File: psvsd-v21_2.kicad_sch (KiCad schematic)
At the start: 28 parts, among them J1 MEM2075-00-140-01-A, U1 RP2040, U4 W25Q32JVZP, X1 ABM8-272-T3

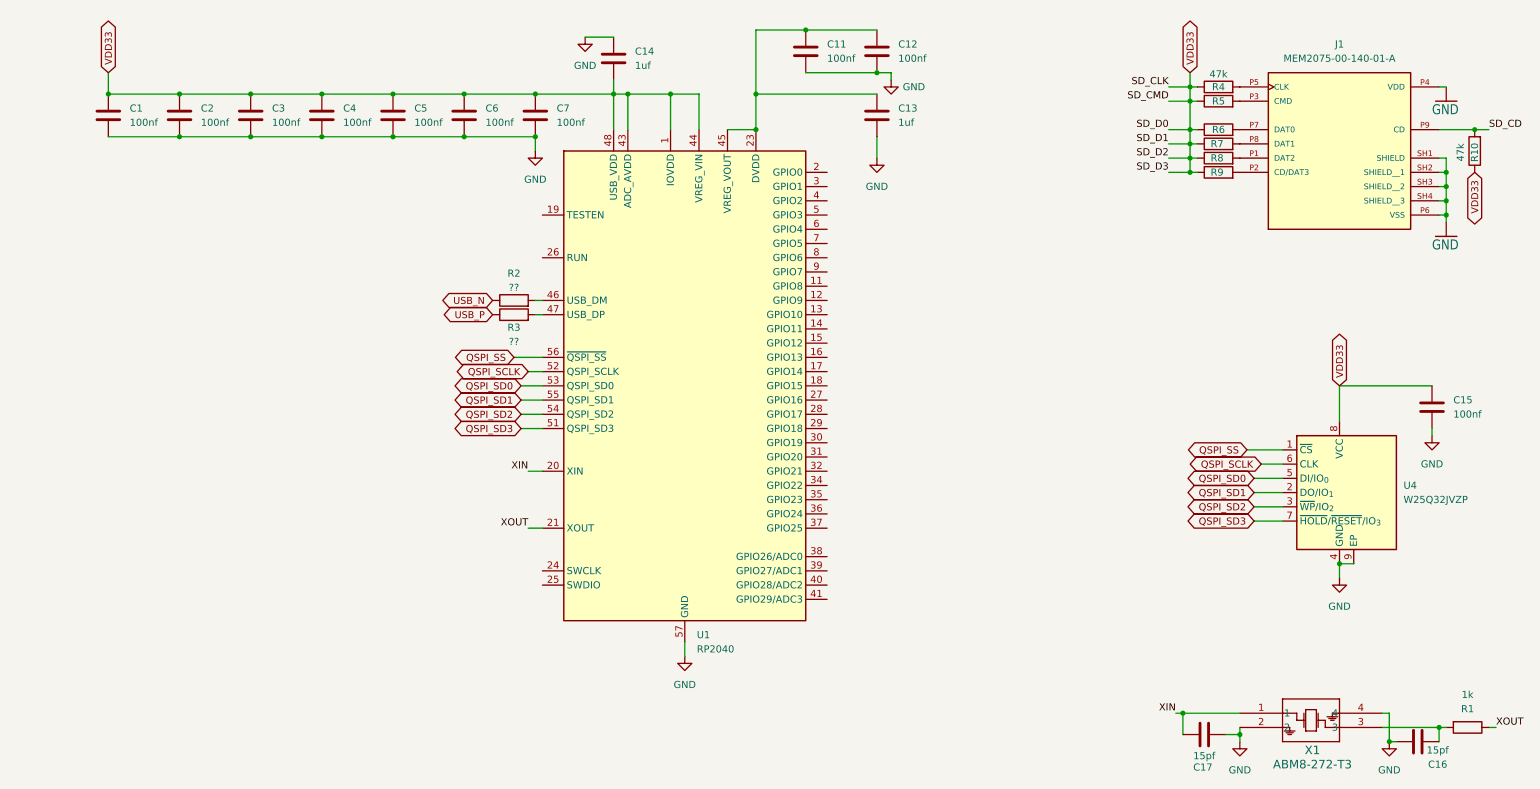
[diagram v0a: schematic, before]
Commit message: Add UART and SWDIO debug headers (plus delete some accidental junk files)
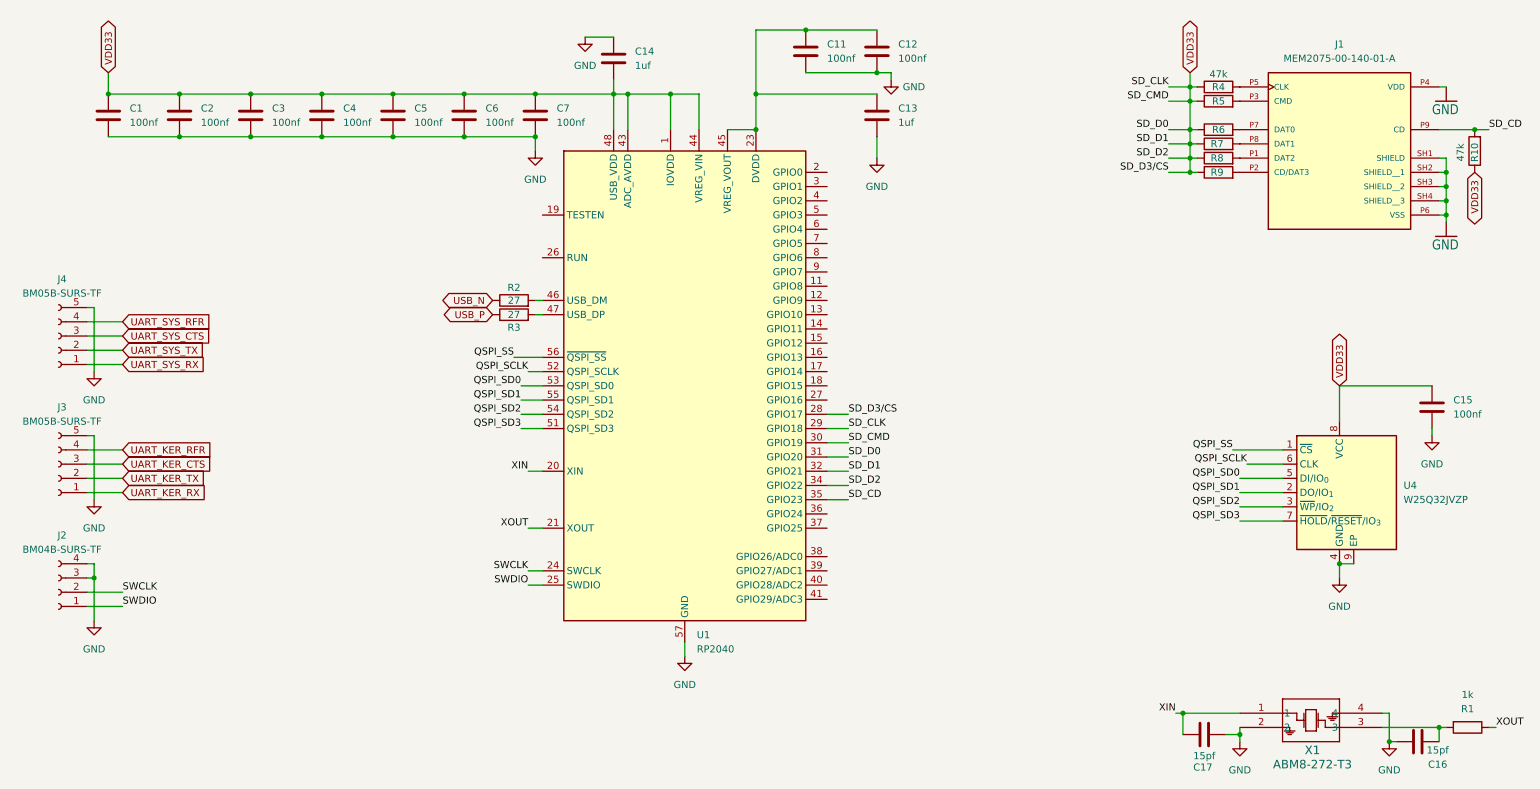
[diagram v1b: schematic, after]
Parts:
- added J2: BM04B-SURS-TF, Connector_JST:JST_SUR_BM04B-SURS-TF_1x04-1MP_P0.80mm_Vertical, symbol Connector:Conn_01x04_Socket
- added J3, J4: BM05B-SURS-TF, Connector_JST:JST_SUR_BM05B-SURS-TF_1x05-1MP_P0.80mm_Vertical, symbol Connector:Conn_01x05_Socket
- R2, R3: value ?? -> 27
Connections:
- net GND: now also J2.3 (Pin_3), J2.4 (Pin_4), J3.5 (Pin_5), J4.5 (Pin_5)
- net SD_CD: now also U1.35 (GPIO23)
- net VDD33: now also U1.28 (GPIO17), U1.29 (GPIO18), U1.30 (GPIO19), U1.31 (GPIO20), U1.32 (GPIO21), U1.34 (GPIO22)
- net SWCLK: now reaches U1.24 (SWCLK)
- net SWCLK: now also J2.2 (Pin_2)
- net SWDIO: now reaches U1.25 (SWDIO)
- net SWDIO: now also J2.1 (Pin_1)
- new net UART_KER_CTS: J3.3 (Pin_3)
- new net UART_KER_RFR: J3.4 (Pin_4)
- new net UART_KER_RX: J3.1 (Pin_1)
- new net UART_KER_TX: J3.2 (Pin_2)
- new net UART_SYS_CTS: J4.3 (Pin_3)
- new net UART_SYS_RFR: J4.4 (Pin_4)
- new net UART_SYS_RX: J4.1 (Pin_1)
- new net UART_SYS_TX: J4.2 (Pin_2)

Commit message: Connect Kermit and Syscon debug headers
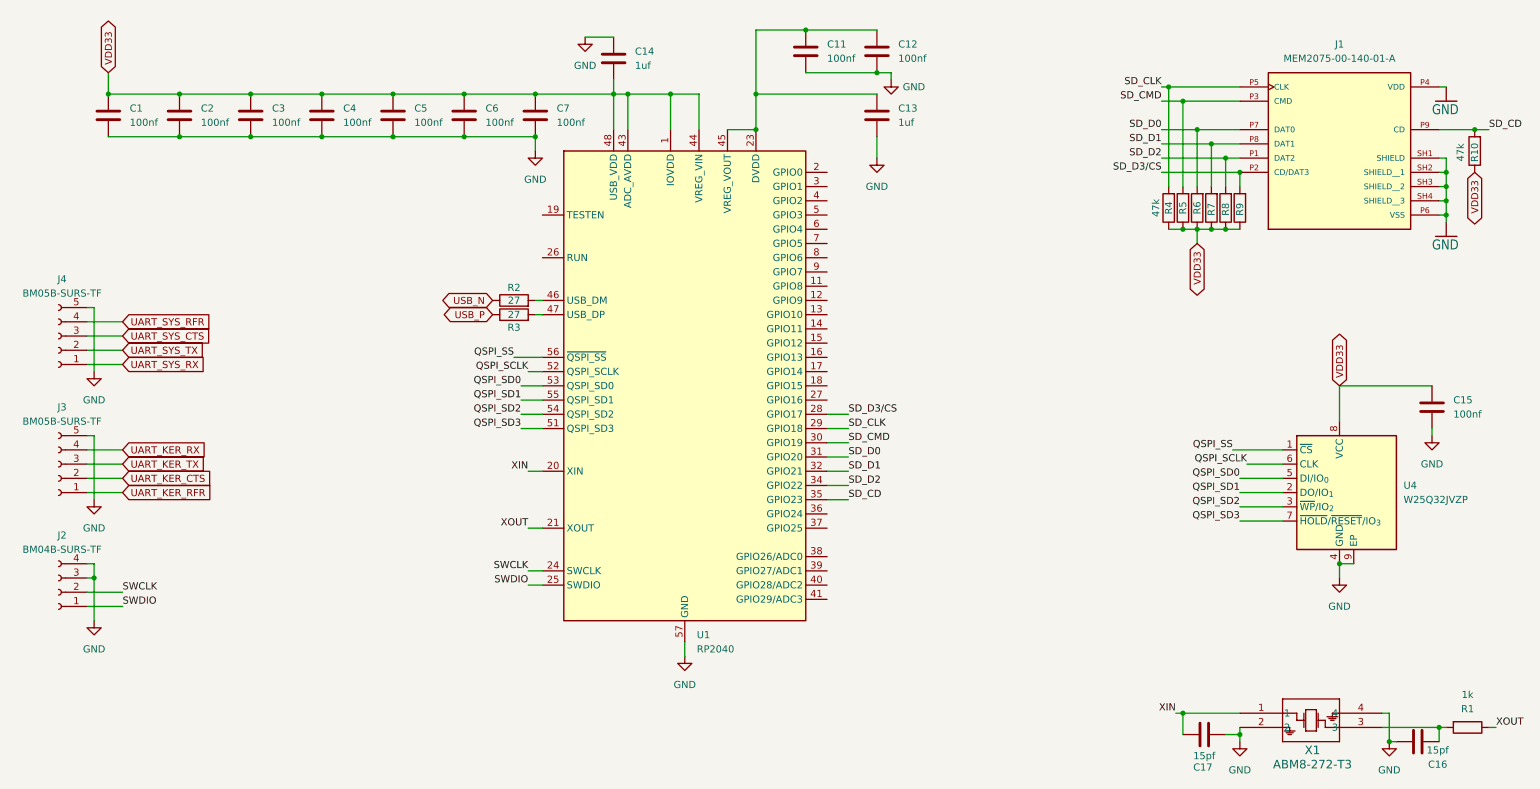
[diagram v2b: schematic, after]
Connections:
- net UART_KER_CTS: now also J3.2 (Pin_2); no longer J3.3 (Pin_3)
- net UART_KER_RFR: now also J3.1 (Pin_1); no longer J3.4 (Pin_4)
- net UART_KER_RX: now also J3.4 (Pin_4); no longer J3.1 (Pin_1)
- net UART_KER_TX: now also J3.3 (Pin_3); no longer J3.2 (Pin_2)
- net VDD33: no longer U1.28 (GPIO17), U1.29 (GPIO18), U1.30 (GPIO19), U1.31 (GPIO20), U1.32 (GPIO21), U1.34 (GPIO22)
- net SD_D2: now reaches J1.P1 (DAT2), R8.2
- net SD_D2: now also U1.34 (GPIO22)
- net SD_D0: now reaches J1.P7 (DAT0), R6.2
- net SD_D0: now also U1.31 (GPIO20)
- net SD_D3/CS: now reaches J1.P2 (CD/DAT3), R9.2
- net SD_D3/CS: now also U1.28 (GPIO17)
- net SD_CLK: now reaches J1.P5 (CLK), R4.2
- net SD_CLK: now also U1.29 (GPIO18)
- net SD_CMD: now reaches J1.P3 (CMD), R5.2
- net SD_CMD: now also U1.30 (GPIO19)
- net SD_D1: now reaches J1.P8 (DAT1), R7.2
- net SD_D1: now also U1.32 (GPIO21)
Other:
- moved on the sheet: R4, R5, R6, R7, R8, R9

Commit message: Fix wrong resistor package
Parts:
- R10: footprint Resistor_SMD:R_0402_1005Metric -> Resistor_SMD:R_01005_0402Metric
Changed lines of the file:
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@@
 			)
 		)
-		(property "Footprint" "Resistor_SMD:R_0402_1005Metric"
+		(property "Footprint" "Resistor_SMD:R_01005_0402Metric"
 			(at 277.368 39.37 90)
 			(hide yes)

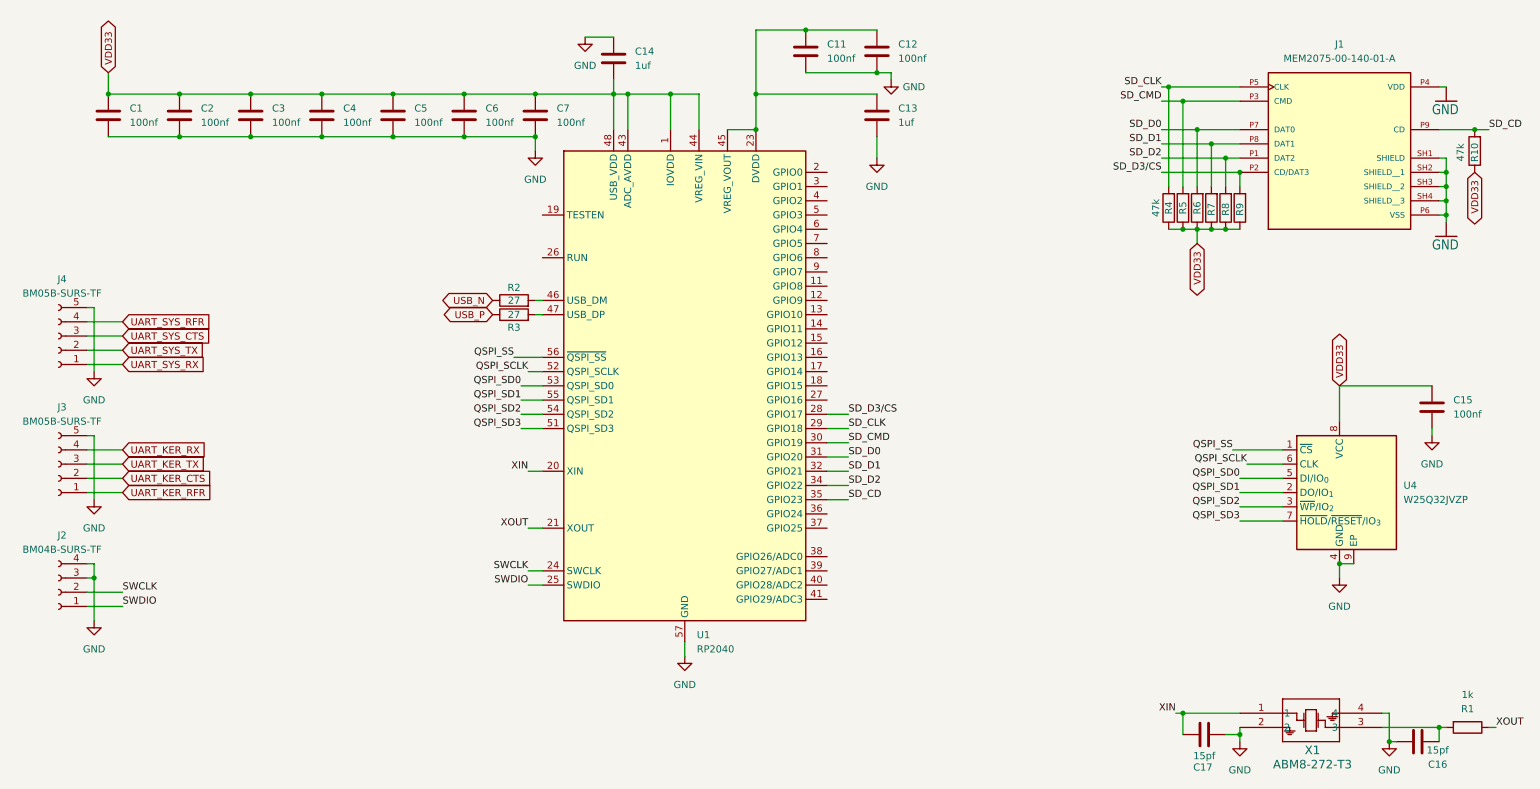
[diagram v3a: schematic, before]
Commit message: Improved layout to reduce reflections
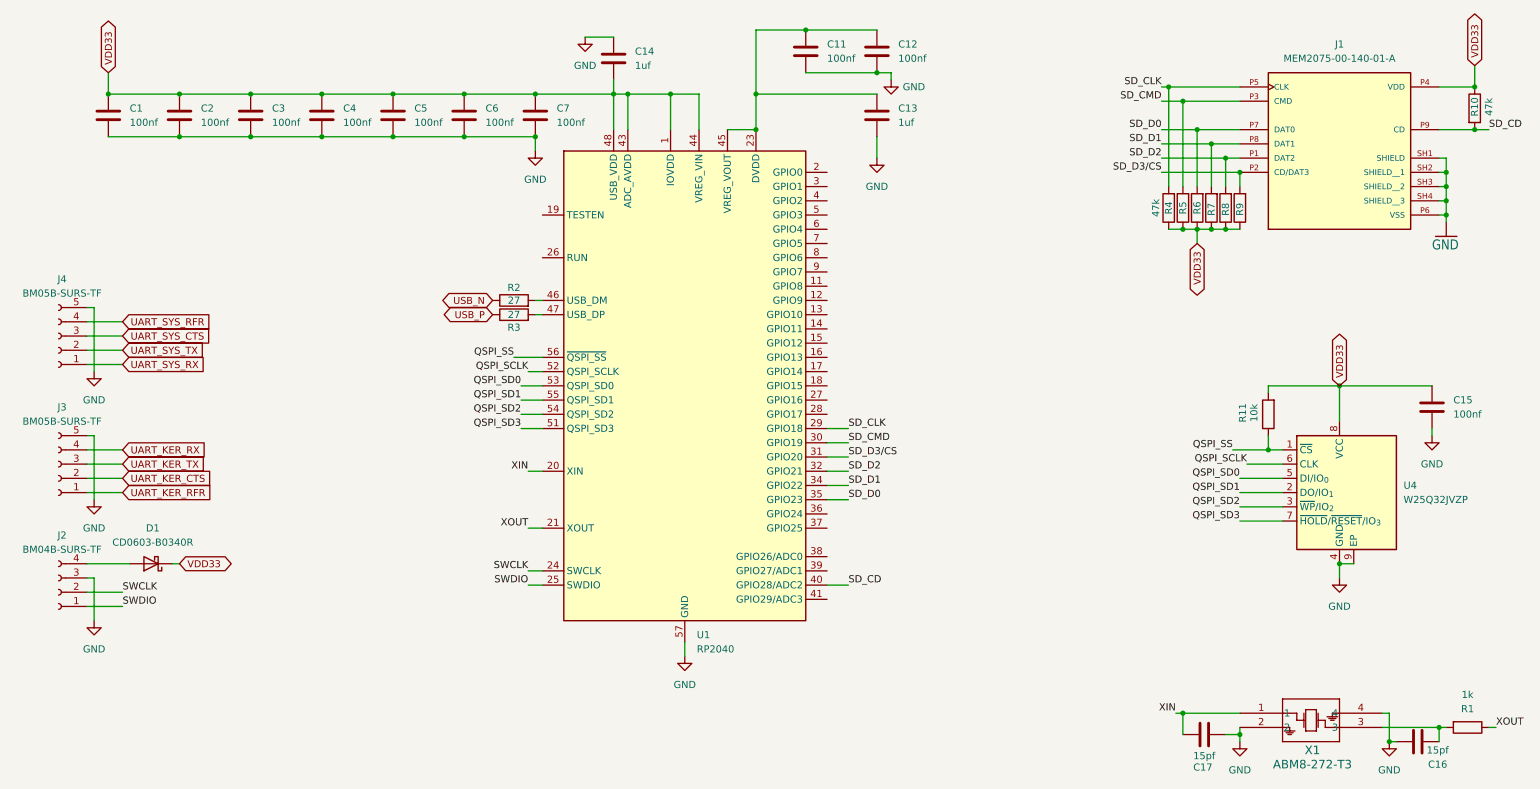
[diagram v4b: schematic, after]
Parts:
- added D1: CD0603-B0340R, symbol Device:D_Schottky
- added R11: 10k, Resistor_SMD:R_01005_0402Metric, symbol Device:R
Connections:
- net GND: no longer J1.P4 (VDD), J2.4 (Pin_4)
- net QSPI_SS: now also R11.1
- net SD_CD: now also U1.40 (GPIO28/ADC2); no longer U1.35 (GPIO23)
- net SD_D0: now also U1.35 (GPIO23); no longer U1.31 (GPIO20)
- net SD_D1: now also U1.34 (GPIO22); no longer U1.32 (GPIO21)
- net SD_D2: now also U1.32 (GPIO21); no longer U1.34 (GPIO22)
- net SD_D3/CS: now also U1.31 (GPIO20); no longer U1.28 (GPIO17)
- net VDD33: now also J1.P4 (VDD), D1.1 (K), R11.2
- new net: D1.2 (A), J2.4 (Pin_4)
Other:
- moved on the sheet: R10

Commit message: Added external 3.3v supply for debug (with backflow diodes)
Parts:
- D1: footprint (none) -> Diode_SMD:D_0603_1608Metric
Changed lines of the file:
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@@
 			)
 		)
-		(property "Footprint" ""
+		(property "Footprint" "Diode_SMD:D_0603_1608Metric"
 			(at 39.37 113.03 0)
 			(hide yes)

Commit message: Increased size of footprints to comply with more fab houses.
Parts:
- C1, C11, C12, C13, C14, C15, C16, C17, C2, C3, C4, C5, C6, C7: footprint Capacitor_SMD:C_01005_0402Metric -> Capacitor_SMD:C_0402_1005Metric_Pad0.74x0.62mm_HandSolder
- R1: footprint Resistor_SMD:R_0402_1005Metric -> Resistor_SMD:R_0402_1005Metric_Pad0.72x0.64mm_HandSolder
- R10, R11, R4, R5, R6, R7, R8, R9: footprint Resistor_SMD:R_01005_0402Metric -> Resistor_SMD:R_0402_1005Metric_Pad0.72x0.64mm_HandSolder
- R2, R3: footprint Resistor_SMD:R_0201_0603Metric -> Resistor_SMD:R_0402_1005Metric_Pad0.72x0.64mm_HandSolder
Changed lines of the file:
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@@
 			)
 		)
-		(property "Footprint" "Capacitor_SMD:C_01005_0402Metric"
+		(property "Footprint" "Capacitor_SMD:C_0402_1005Metric_Pad0.74x0.62mm_HandSolder"
 			(at 70.8152 36.83 0)
 			(hide yes)
@@
 			)
 		)
-		(property "Footprint" "Resistor_SMD:R_01005_0402Metric"
+		(property "Footprint" "Resistor_SMD:R_0402_1005Metric_Pad0.72x0.64mm_HandSolder"
 			(at 232.918 49.53 90)
 			(hide yes)
@@
 			)
 		)
-		(property "Footprint" "Resistor_SMD:R_01005_0402Metric"
+		(property "Footprint" "Resistor_SMD:R_0402_1005Metric_Pad0.72x0.64mm_HandSolder"
 			(at 273.812 31.75 90)
 			(hide yes)
@@
 			)
 		)
-		(property "Footprint" "Resistor_SMD:R_01005_0402Metric"
+		(property "Footprint" "Resistor_SMD:R_0402_1005Metric_Pad0.72x0.64mm_HandSolder"
 			(at 227.838 49.53 90)
 			(hide yes)
@@
 			)
 		)
-		(property "Footprint" "Capacitor_SMD:C_01005_0402Metric"
+		(property "Footprint" "Capacitor_SMD:C_0402_1005Metric_Pad0.74x0.62mm_HandSolder"
 			(at 32.7152 36.83 0)
 			(hide yes)
@@
 			)
 		)
-		(property "Footprint" "Capacitor_SMD:C_01005_0402Metric"
+		(property "Footprint" "Capacitor_SMD:C_0402_1005Metric_Pad0.74x0.62mm_HandSolder"
 			(at 83.5152 36.83 0)
 			(hide yes)
@@
 			)
 		)
-		(property "Footprint" "Capacitor_SMD:C_01005_0402Metric"
+		(property "Footprint" "Capacitor_SMD:C_0402_1005Metric_Pad0.74x0.62mm_HandSolder"
 			(at 58.1152 36.83 0)
 			(hide yes)
@@
 			)
 		)
-		(property "Footprint" "Resistor_SMD:R_0402_1005Metric"
+		(property "Footprint" "Resistor_SMD:R_0402_1005Metric_Pad0.72x0.64mm_HandSolder"
 			(at 274.32 140.462 90)
 			(hide yes)
@@
 			)
 		)
-		(property "Footprint" "Capacitor_SMD:C_01005_0402Metric"
+		(property "Footprint" "Capacitor_SMD:C_0402_1005Metric_Pad0.74x0.62mm_HandSolder"
 			(at 268.9352 88.9 0)
 			(hide yes)
@@
 			)
 		)
-		(property "Footprint" "Resistor_SMD:R_01005_0402Metric"
+		(property "Footprint" "Resistor_SMD:R_0402_1005Metric_Pad0.72x0.64mm_HandSolder"
 			(at 235.458 49.53 90)
 			(hide yes)
@@
 			)
 		)
-		(property "Footprint" "Capacitor_SMD:C_01005_0402Metric"
+		(property "Footprint" "Capacitor_SMD:C_0402_1005Metric_Pad0.74x0.62mm_HandSolder"
 			(at 269.24 143.8148 0)
 			(hide yes)
@@
 			)
 		)
-		(property "Footprint" "Capacitor_SMD:C_01005_0402Metric"
+		(property "Footprint" "Capacitor_SMD:C_0402_1005Metric_Pad0.74x0.62mm_HandSolder"
 			(at 96.2152 36.83 0)
 			(hide yes)
@@
 			)
 		)
-		(property "Footprint" "Capacitor_SMD:C_01005_0402Metric"
+		(property "Footprint" "Capacitor_SMD:C_0402_1005Metric_Pad0.74x0.62mm_HandSolder"
 			(at 223.52 144.4752 0)
 			(hide yes)
@@
 			)
 		)
-		(property "Footprint" "Capacitor_SMD:C_01005_0402Metric"
+		(property "Footprint" "Capacitor_SMD:C_0402_1005Metric_Pad0.74x0.62mm_HandSolder"
 			(at 169.8752 36.83 0)
 			(hide yes)
@@
 			)
 		)
-		(property "Footprint" "Resistor_SMD:R_0201_0603Metric"
+		(property "Footprint" "Resistor_SMD:R_0402_1005Metric_Pad0.72x0.64mm_HandSolder"
 			(at 104.14 67.818 90)
 			(hide yes)
@@
 			)
 		)
-		(property "Footprint" "Resistor_SMD:R_01005_0402Metric"
+		(property "Footprint" "Resistor_SMD:R_0402_1005Metric_Pad0.72x0.64mm_HandSolder"
 			(at 240.538 86.36 90)
 			(hide yes)
@@
 			)
 		)
-		(property "Footprint" "Resistor_SMD:R_01005_0402Metric"
+		(property "Footprint" "Resistor_SMD:R_0402_1005Metric_Pad0.72x0.64mm_HandSolder"
 			(at 222.758 49.53 90)
 			(hide yes)
@@
 			)
 		)
-		(property "Footprint" "Capacitor_SMD:C_01005_0402Metric"
+		(property "Footprint" "Capacitor_SMD:C_0402_1005Metric_Pad0.74x0.62mm_HandSolder"
 			(at 122.8852 26.67 0)
 			(hide yes)
@@
 			)
 		)
-		(property "Footprint" "Resistor_SMD:R_01005_0402Metric"
+		(property "Footprint" "Resistor_SMD:R_0402_1005Metric_Pad0.72x0.64mm_HandSolder"
 			(at 225.298 49.53 90)
 			(hide yes)
@@
 			)
 		)
-		(property "Footprint" "Capacitor_SMD:C_01005_0402Metric"
+		(property "Footprint" "Capacitor_SMD:C_0402_1005Metric_Pad0.74x0.62mm_HandSolder"
 			(at 169.8752 25.4 0)
 			(hide yes)
@@
 			)
 		)
-		(property "Footprint" "Resistor_SMD:R_01005_0402Metric"
+		(property "Footprint" "Resistor_SMD:R_0402_1005Metric_Pad0.72x0.64mm_HandSolder"
 			(at 230.378 49.53 90)
 			(hide yes)
@@
 			)
 		)
-		(property "Footprint" "Capacitor_SMD:C_01005_0402Metric"
+		(property "Footprint" "Capacitor_SMD:C_0402_1005Metric_Pad0.74x0.62mm_HandSolder"
 			(at 157.1752 25.4 0)
 			(hide yes)
@@
 			)
 		)
-		(property "Footprint" "Capacitor_SMD:C_01005_0402Metric"
+		(property "Footprint" "Capacitor_SMD:C_0402_1005Metric_Pad0.74x0.62mm_HandSolder"
 			(at 108.9152 36.83 0)
 			(hide yes)
@@
 			)
 		)
-		(property "Footprint" "Resistor_SMD:R_0201_0603Metric"
+		(property "Footprint" "Resistor_SMD:R_0402_1005Metric_Pad0.72x0.64mm_HandSolder"
 			(at 104.14 70.358 90)
 			(hide yes)
@@
 			)
 		)
-		(property "Footprint" "Capacitor_SMD:C_01005_0402Metric"
+		(property "Footprint" "Capacitor_SMD:C_0402_1005Metric_Pad0.74x0.62mm_HandSolder"
 			(at 45.4152 36.83 0)
 			(hide yes)
